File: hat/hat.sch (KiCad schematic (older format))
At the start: 0 parts

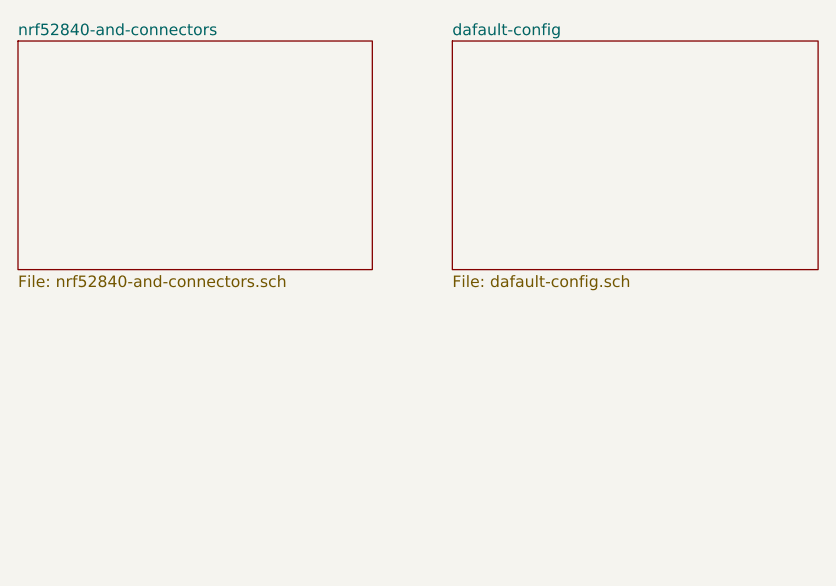
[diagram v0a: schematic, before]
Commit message: started external power input schematic
-please note this is not edited to be right it just has all the parts added based off the diagram in the lm2676 datasheet 
-power link it rpi added
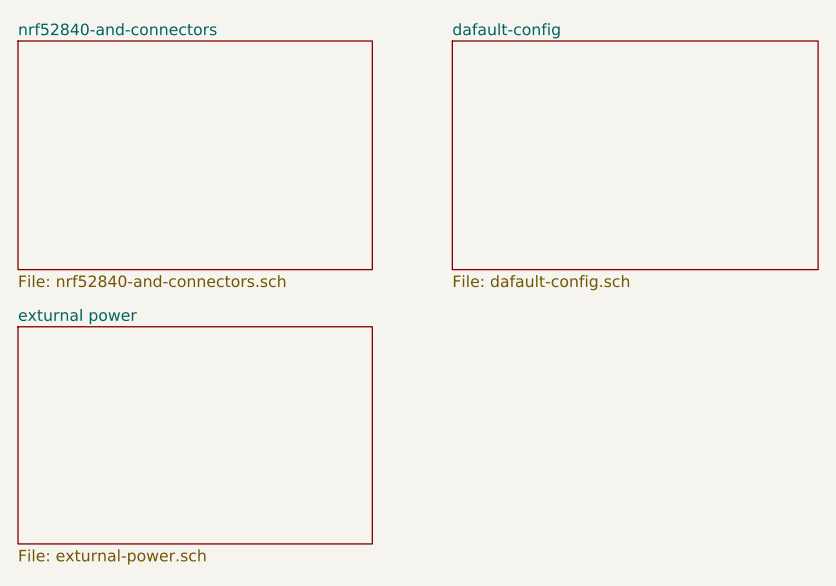
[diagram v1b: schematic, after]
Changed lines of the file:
@@
 $Descr A4 11693 8268
 encoding utf-8
-Sheet 1 3
+Sheet 1 4
 Title ""
 Date ""
@@
 F1 "nrf52840-and-connectors.sch" 50
 $EndSheet
+$Sheet
+S 1000 2200 1550 950
+U 5C7E653E
+F0 "exturnal power" 50
+F1 "exturnal-power.sch" 50
+$EndSheet
 $EndSCHEMATC
